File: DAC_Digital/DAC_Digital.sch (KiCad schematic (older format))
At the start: 131 parts, among them J1 +5V_in, J10 USB_Dev4, J11 P9, J12 Anlg_in, J13 Anlg_I2C, J14 P8, J15 Test, J16 Test, J17 Fix, J18 Fix, J19 Fix, J2 DBG_PORT, J20 Fix, J3 DSPL_PORT, J4 Out_SPDIF, J5 USB0, J6 USB1, J7 USB_Dev1, J8 USB_Dev2, J9 USB_Dev3, Q1 2n7002, Q2 2N7002, Q3 FDS4435, Q4 FDS4435, Q5 2N7002, Q6 2N7002, T1 DA103C, U1 CS8406_2, U2 PIC18F6722, U3 74LVC1G08GW, U4 PCM2903C, U5 74LVC1G08GW, U6 USB2514B-AEZC, U7 NE5532, X1 7A-24.000MAAJ-T, Y1 10MHz, Y2 12MHz

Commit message: Update schematic
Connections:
- wire segments 547 -> 551
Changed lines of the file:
@@
 L Conn_01x04 J5
 U 1 1 59D63510
-P 9700 11900
-F 0 "J5" H 9700 12100 50  0000 C CNN
-F 1 "USB0" H 9700 11600 50  0000 C CNN
-F 2 "Pin_Headers:Pin_Header_Straight_1x04_Pitch2.54mm" H 9700 11900 50  0001 C CNN
-F 3 "" H 9700 11900 50  0001 C CNN
-	1    9700 11900
+P 9450 11900
+F 0 "J5" H 9450 12100 50  0000 C CNN
+F 1 "USB0" H 9450 11600 50  0000 C CNN
+F 2 "Pin_Headers:Pin_Header_Straight_1x04_Pitch2.54mm" H 9450 11900 50  0001 C CNN
+F 3 "" H 9450 11900 50  0001 C CNN
+	1    9450 11900
 	-1   0    0    1
 $EndComp
@@
 	1    0    0    -1
 $EndComp
-Text Label 15450 10850 0    60   ~ 0
-Vanlg
-Text Label 15450 12400 0    60   ~ 0
-Vanlg
 $Comp
 L GNDD #PWR29
@@
 	10600 12250 10950 12250
 Wire Wire Line
-	10600 11800 9900 11800
-Wire Wire Line
-	9900 11900 10800 11900
+	10600 11800 9650 11800
+Wire Wire Line
+	9650 11900 10800 11900
 Wire Wire Line
 	10800 11650 10800 12000
 Wire Wire Line
 	10800 12000 10950 12000
-Wire Wire Line
-	9900 12000 9900 12100
 Connection ~ 10800 11900
 Wire Wire Line
@@
 Wire Wire Line
 	9950 11300 9950 11700
-Connection ~ 9950 11700
 Wire Wire Line
 	10400 11700 10400 12850
@@
 	12250 14400 12250 14450
 Connection ~ 12250 14450
-Wire Wire Line
-	9900 11700 10400 11700
 Wire Wire Line
 	10850 12650 11400 12650
@@
 	1    0    0    -1
 $EndComp
+Text Label 15450 10850 0    50   ~ 10
++5v_Dev
+Text Label 15450 12400 0    50   ~ 10
++5v_Dev
+Wire Wire Line
+	9650 12000 9900 12000
+Wire Wire Line
+	9900 12000 9900 12100
+Wire Wire Line
+	9950 11700 10400 11700
+Text Label 9400 11450 0    60   ~ 0
+VDD_5V
+Wire Wire Line
+	9400 11450 9750 11450
+Wire Wire Line
+	9750 11450 9750 11700
+Wire Wire Line
+	9750 11700 9650 11700
 $EndSCHEMATC

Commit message: Update gnd connection on digital transformer
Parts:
- R11: value 91 -> 390
- R40: value 390 -> 91
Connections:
- net labels added: /CS, IntB, IntIR, MISO, MOSI, SCK
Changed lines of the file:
@@
 P 7850 15250
 F 0 "R11" V 7930 15250 50  0000 C CNN
-F 1 "91" V 7850 15250 50  0000 C CNN
+F 1 "390" V 7850 15250 50  0000 C CNN
 F 2 "Yame_library:SM0603-MR" V 7780 15250 50  0001 C CNN
 F 3 "" H 7850 15250 50  0001 C CNN
@@
 P 13850 13200
 F 0 "R40" V 13930 13200 50  0000 C CNN
-F 1 "390" V 13850 13200 50  0000 C CNN
+F 1 "91" V 13850 13200 50  0000 C CNN
 F 2 "Yame_library:SM0603-MR" V 13780 13200 50  0001 C CNN
 F 3 "" H 13850 13200 50  0001 C CNN
@@
 Wire Wire Line
 	9750 11700 9650 11700
+Text Label 7950 5300 0    60   ~ 0
+IntB
+Text Label 7950 5200 0    60   ~ 0
+IntIR
+Text Label 8000 5400 0    60   ~ 0
+MOSI
+Text Label 8050 5500 0    60   ~ 0
+MISO
+Text Label 8100 5600 0    60   ~ 0
+SCK
+Text Label 8150 5700 0    60   ~ 0
+/CS
 $EndSCHEMATC

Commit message: Create MIG project
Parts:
- added R?: 10k, Yame_library:SM0603-MR, symbol DAC_Digital-rescue:R
- C1, C10, C11, C12, C13, C14, C15, C16, C2, C20, C21, C22, C23, C24, C26, C29, C3, C33, C34, C38, C39, C4, C40, C41, C42, C43, C44, C5, C6, C7, C8, C9: symbol C -> DAC_Digital-rescue:C
- C17, C18, C19, C25, C27, C28, C30, C31, C32, C35, C36, C37, C45, C46, C47, C48: symbol C-RESCUE-EPM_V5 -> DAC_Digital-rescue:C-RESCUE-EPM_V5
- D1: symbol D_TVS -> DAC_Digital-rescue:D_TVS
- D2, D3: symbol LED -> DAC_Digital-rescue:LED
- F1: symbol FUSE_CLIP_5x20 -> YameLib:FUSE_CLIP_5x20
- J1, J4: symbol Conn_01x02 -> DAC_Digital-rescue:Conn_01x02
- J10, J12, J13, J5, J6, J7, J8, J9: symbol Conn_01x04 -> DAC_Digital-rescue:Conn_01x04
- J11, J14: symbol Conn_02x23_Odd_Even -> DAC_Digital-rescue:Conn_02x23_Odd_Even
- J15, J16, J3: symbol Conn_01x08 -> DAC_Digital-rescue:Conn_01x08
- J17, J18, J19, J20: symbol Conn_01x01 -> DAC_Digital-rescue:Conn_01x01
- J2: symbol Conn_01x05 -> DAC_Digital-rescue:Conn_01x05
- L1, L2: symbol L_Core_Ferrite -> DAC_Digital-rescue:L_Core_Ferrite
- Q1, Q2: symbol N-MOS_SOT23 -> YameLib:N-MOS_SOT23
- Q3, Q4: symbol P-MOS_SOIC -> YameLib:P-MOS_SOIC
- Q5, Q6: symbol 2N7002 -> DAC_Digital-rescue:2N7002
- R1, R10, R11, R12, R13, R14, R15, R16, R17, R18, R19, R2, R20, R27, R28, R29, R3, R30, R31, R32, R33, R34, R35, R36, R37, R38, R39, R4, R40, R5: symbol R -> DAC_Digital-rescue:R
- R21, R22, R23, R24, R25, R26, R6, R7, R8, R9: symbol R-RESCUE-EPM_V5 -> DAC_Digital-rescue:R-RESCUE-EPM_V5
- T1: symbol DA103C -> YameLib:DA103C
- U1: symbol CS8406_2 -> YameLib:CS8406_2
- U2: symbol PIC18F6722 -> YameLib:PIC18F6722
- U3, U5: symbol 74AHC1G08 -> DAC_Digital-rescue:74AHC1G08
- U4: symbol PCM2903C -> YameLib:PCM2903C
- U6: symbol USB2514B -> YameLib:USB2514B
- U7: symbol OPA2333xxD -> DAC_Digital-rescue:OPA2333xxD
- X1: symbol CMJ206T32.768KDZF-UT -> YameLib:CMJ206T32.768KDZF-UT
- Y1, Y2: symbol Crystal -> DAC_Digital-rescue:Crystal
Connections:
- wire segments 551 -> 660

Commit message: Update DAC digital board, switch to odroid C2
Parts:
- removed C1, C14, C2, C29, C3, C5: 100n, Yame_library:SM0603-MR, symbol DAC_Digital-rescue:C
- removed C13: 100u, Capacitors_Tantalum_SMD:CP_Tantalum_Case-U_EIA-6032-15_Hand, symbol DAC_Digital-rescue:C
- removed C15, C16: 18p, Yame_library:SM0603-MR, symbol DAC_Digital-rescue:C
- removed C17, C19: 18p, Yame_library:SM0402-MR, symbol DAC_Digital-rescue:C-RESCUE-EPM_V5
- removed C18, C27, C28, C30, C31, C32, C35, C36, C37: 100n, Yame_library:SM0402-MR, symbol DAC_Digital-rescue:C-RESCUE-EPM_V5
- removed C20, C21, C22, C23, C24, C26, C33, C34, C40, C43, C44: 10u, Yame_library:SM0805-MR, symbol DAC_Digital-rescue:C
- removed C25, C45, C46, C47, C48: 10u, Yame_library:SM0805-MR, symbol DAC_Digital-rescue:C-RESCUE-EPM_V5
- removed C38, C39, C41, C42: 330p, Yame_library:SM0603-MR, symbol DAC_Digital-rescue:C
- removed J10: USB_Dev4, Pin_Headers:Pin_Header_Straight_1x04_Pitch2.54mm, symbol DAC_Digital-rescue:Conn_01x04
- removed J11: P9, Pin_Headers:Pin_Header_Straight_2x23_Pitch2.54mm, symbol DAC_Digital-rescue:Conn_02x23_Odd_Even
- removed J12: Anlg_in, Pin_Headers:Pin_Header_Straight_1x04_Pitch2.54mm, symbol DAC_Digital-rescue:Conn_01x04
- removed J14: P8, Pin_Headers:Pin_Header_Straight_2x23_Pitch2.54mm, symbol DAC_Digital-rescue:Conn_02x23_Odd_Even
- removed J15, J16: Test, Pin_Headers:Pin_Header_Straight_1x08_Pitch1.27mm, symbol DAC_Digital-rescue:Conn_01x08
- removed J17, J18, J19, J20: Fix, Mounting_Holes:MountingHole_3.2mm_M3, symbol DAC_Digital-rescue:Conn_01x01
- removed J5: USB0, Pin_Headers:Pin_Header_Straight_1x04_Pitch2.54mm, symbol DAC_Digital-rescue:Conn_01x04
- removed J6: USB1, Pin_Headers:Pin_Header_Straight_1x04_Pitch2.54mm, symbol DAC_Digital-rescue:Conn_01x04
- removed J7: USB_Dev1, Pin_Headers:Pin_Header_Straight_1x04_Pitch2.54mm, symbol DAC_Digital-rescue:Conn_01x04
- removed J8: USB_Dev2, Pin_Headers:Pin_Header_Straight_1x04_Pitch2.54mm, symbol DAC_Digital-rescue:Conn_01x04
- removed J9: USB_Dev3, Pin_Headers:Pin_Header_Straight_1x04_Pitch2.54mm, symbol DAC_Digital-rescue:Conn_01x04
- removed L1, L2: BLM18AG102SN1D, Yame_library:SM0603-MR, symbol DAC_Digital-rescue:L_Core_Ferrite
- removed Q2: 2N7002, Yame_library:SOT23-MR, symbol YameLib:N-MOS_SOT23
- removed Q4: FDS4435, Housings_SOIC:SOIC-8_3.9x4.9mm_Pitch1.27mm, symbol YameLib:P-MOS_SOIC
- removed R1, R2, R3: R, Yame_library:SM0603-MR, symbol DAC_Digital-rescue:R
- removed R10, R11: 390, Yame_library:SM0603-MR, symbol DAC_Digital-rescue:R
- removed R16, R17: 1M, Yame_library:SM0603-MR, symbol DAC_Digital-rescue:R
- removed R18: 1,5k, Yame_library:SM0603-MR, symbol DAC_Digital-rescue:R
- removed R19, R20: 22, Yame_library:SM0603-MR, symbol DAC_Digital-rescue:R
- removed R21, R22, R23, R24, R25: 47k, Yame_library:SM0402-MR, symbol DAC_Digital-rescue:R-RESCUE-EPM_V5
- removed R26: 12k, Yame_library:SM0402-MR, symbol DAC_Digital-rescue:R-RESCUE-EPM_V5
- removed R27, R28: 100, Yame_library:SM0603-MR, symbol DAC_Digital-rescue:R
- removed R29, R30, R33, R34: 12k, Yame_library:SM0603-MR, symbol DAC_Digital-rescue:R
- removed R31, R32: 3.9k, Yame_library:SM0603-MR, symbol DAC_Digital-rescue:R
- removed R39: 1meg, Yame_library:SM0603-MR, symbol DAC_Digital-rescue:R
- removed R40: 91, Yame_library:SM0603-MR, symbol DAC_Digital-rescue:R
- removed R5: 47k, Yame_library:SM0603-MR, symbol DAC_Digital-rescue:R
- removed R7, R9: 1meg, Yame_library:SM0603-MR, symbol DAC_Digital-rescue:R-RESCUE-EPM_V5
- removed T1: DA103C, Housings_DIP:DIP-6_W10.16mm, symbol YameLib:DA103C
- removed U1: CS8406_2, Housings_SOIC:SOIC-28W_7.5x18.7mm_Pitch1.27mm, symbol YameLib:CS8406_2
- removed U3, U5: 74LVC1G08GW, TO_SOT_Packages_SMD:SOT-353_SC-70-5, symbol DAC_Digital-rescue:74AHC1G08
- removed U4: PCM2903C, Housings_SSOP:SSOP-28_5.3x10.2mm_Pitch0.65mm, symbol YameLib:PCM2903C
- removed U6: USB2514B-AEZC, Housings_DFN_QFN:QFN-36-1EP_6x6mm_Pitch0.5mm, symbol YameLib:USB2514B
- removed U7: NE5532, Housings_SOIC:SOIC-8_3.9x4.9mm_Pitch1.27mm, symbol DAC_Digital-rescue:OPA2333xxD
- removed X1: 7A-24.000MAAJ-T, Yame_library:7A_SERIES_TXC, symbol YameLib:CMJ206T32.768KDZF-UT
- removed Y2: 12MHz, Crystals:Crystal_HC49-4H_Vertical, symbol DAC_Digital-rescue:Crystal
- added J5: Conn_02x20_Odd_Even, Connector_PinSocket_2.54mm:PinSocket_2x20_P2.54mm_Vertical, symbol Connector_Generic:Conn_02x20_Odd_Even
- added J6: Conn_01x07, Connector_PinSocket_2.54mm:PinSocket_1x07_P2.54mm_Vertical, symbol Connector_Generic:Conn_01x07
- C10, C11, C4, C6, C7, C8, C9, R12, R13, R14, R15, R35, R36, R37, R38, R4, R6, R8: footprint Yame_library:SM0603-MR -> Resistor_SMD:R_0603_1608Metric
- D1: footprint Diodes_SMD:D_SMC -> Diode_SMD:D_SMC
- D2: footprint Yame_library:SM0603-LED-MR -> LED_SMD:LED_0603_1608Metric
- D3: footprint Yame_library:SM0603-LED-MR -> Resistor_SMD:R_0603_1608Metric
- F1: footprint Fuse_Holders_and_Fuses:Fuseholder5x20_horiz_open_universal_Type-III -> Yame_library:Fuse_5x20
- J1: footprint Connectors:bornier2 -> TerminalBlock:TerminalBlock_bornier-2_P5.08mm
- Q1, Q5, Q6: footprint Yame_library:SOT23-MR -> Package_TO_SOT_SMD:SOT-23
- Q3: footprint Housings_SOIC:SOIC-8_3.9x4.9mm_Pitch1.27mm -> Package_SO:SO-8_5.3x6.2mm_P1.27mm
- R1: renamed from R?; footprint Yame_library:SM0603-MR -> Resistor_SMD:R_0603_1608Metric
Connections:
- net labels removed: D+_Dev1, D+_Dev2, D+_Dev3, D+_Dev4, D-_Dev1, D-_Dev2, D-_Dev3, D-_Dev4, SPDIF_OUT, VD, VDD_5V_USB1, Vanlg, Vcom
- wire segments 660 -> 233
- no-connect marks 9 -> 0

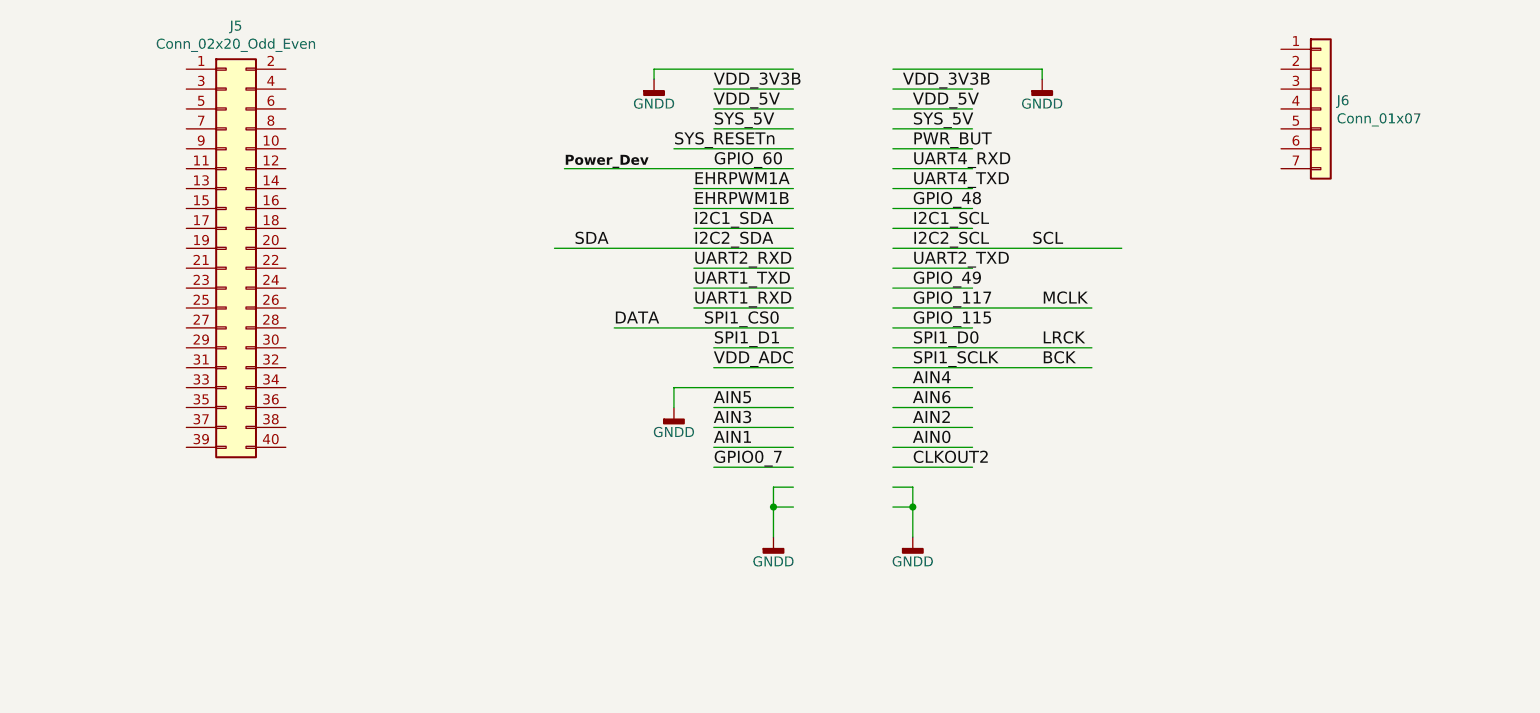
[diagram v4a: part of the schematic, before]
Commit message: Update DAC_Digital sch
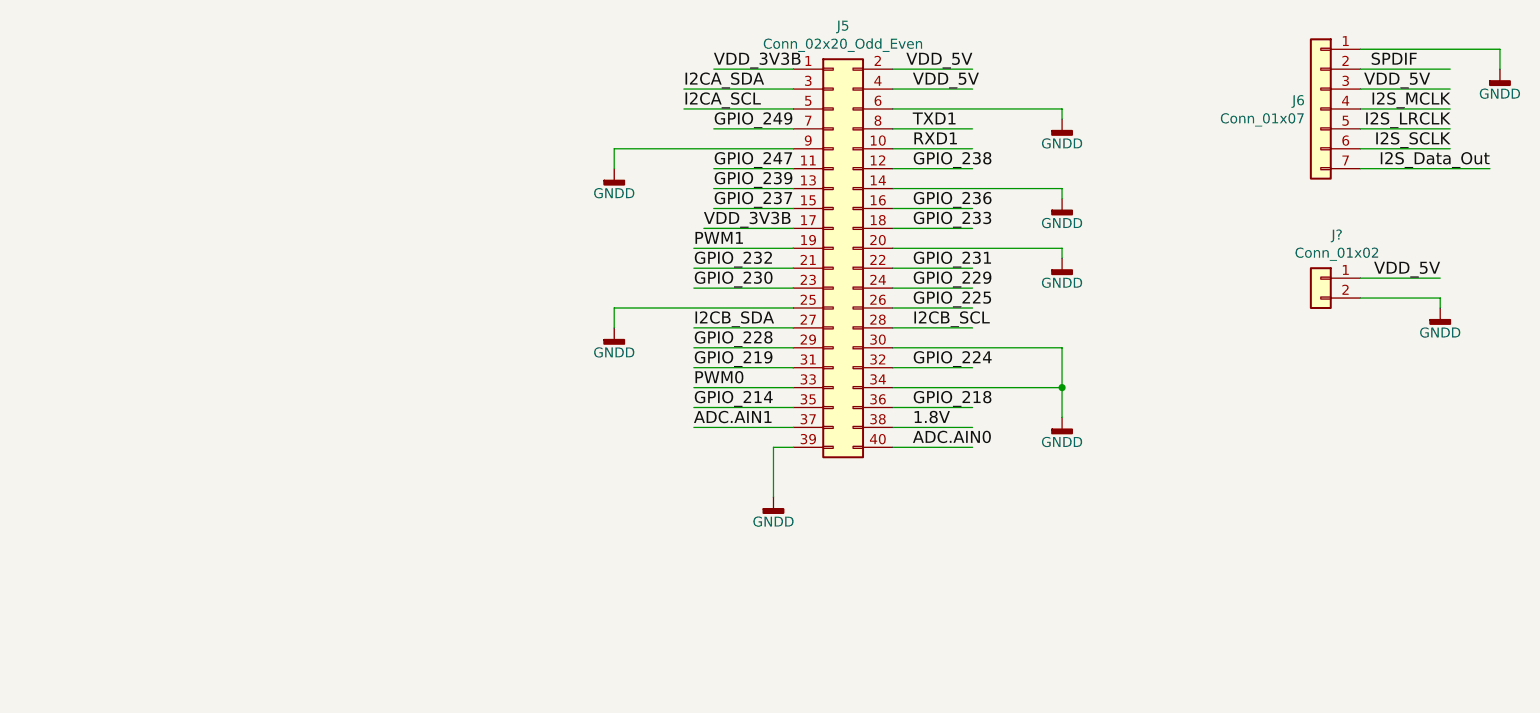
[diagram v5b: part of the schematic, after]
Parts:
- added J?: Conn_01x02, symbol Connector_Generic:Conn_01x02
- D3: footprint Resistor_SMD:R_0603_1608Metric -> LED_SMD:LED_0603_1608Metric
- J13: footprint Pin_Headers:Pin_Header_Straight_1x04_Pitch2.54mm -> Connector_PinHeader_2.54mm:PinHeader_1x04_P2.54mm_Vertical
- J2: footprint Pin_Headers:Pin_Header_Straight_1x05_Pitch2.54mm -> Connector_PinHeader_2.54mm:PinHeader_1x05_P2.54mm_Horizontal
- J3: footprint Pin_Headers:Pin_Header_Straight_1x08_Pitch2.54mm -> Connector_PinHeader_2.54mm:PinHeader_1x08_P2.54mm_Horizontal
- J4: footprint Pin_Headers:Pin_Header_Straight_1x02_Pitch2.54mm -> Connector_PinHeader_2.54mm:PinHeader_1x02_P2.54mm_Vertical
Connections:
- net labels added: 1.8V, ADC.AIN0, ADC.AIN1, GPIO_214, GPIO_218, GPIO_219, GPIO_224, GPIO_225, GPIO_228, GPIO_229, GPIO_230, GPIO_231, GPIO_232, GPIO_233, GPIO_236, GPIO_237, GPIO_238, GPIO_239, GPIO_247, GPIO_249, I2CA_SCL, I2CA_SDA, I2CB_SCL, I2CB_SDA, I2S_Data_Out, I2S_LRCLK, I2S_MCLK, I2S_SCLK, PWM0, PWM1, RXD1, SPDIF, TXD1
- net labels removed: AIN0, AIN1, AIN2, AIN3, AIN4, AIN5, AIN6, BCK, CLKOUT2, DATA, EHRPWM1A, EHRPWM1B, GPIO0_7, GPIO_115, GPIO_117, GPIO_48, GPIO_49, GPIO_60, I2C1_SCL, I2C1_SDA, I2C2_SCL, I2C2_SDA, LRCK, MCLK, PWR_BUT, SPI1_CS0, SPI1_D0, SPI1_D1, SPI1_SCLK, SYS_5V, SYS_RESETn, UART1_RXD, UART1_TXD, UART2_RXD, UART2_TXD, VDD_ADC
- wire segments 233 -> 239
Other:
- moved on the sheet: J5, J6
